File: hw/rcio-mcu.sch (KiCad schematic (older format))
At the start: 0 parts

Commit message: hw: start stm page
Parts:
- added C? (x5): 0.1, symbol Device:C
- added DD?: STM32F030CCTx, Package_QFP:LQFP-48_7x7mm_P0.5mm, symbol MCU_ST_STM32:STM32F030CCTx
- added XP?: stm_swdo, symbol dronecode_con:stm_swdo
- added XP?: FrSky-XSR, symbol dronecode_con:FrSky-XSR
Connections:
- net labels added: +3.3V, ADC_V5hat, ADC_Vbat, GND, HAT_CLK, RPI_SCL, RPI_SDA, RPI_SPI0_MISO, RPI_SPI0_MOSI, RPI_SPI0_SCLK, SERVO0, SERVO1, SERVO2, SERVO3, STM_BOOT0, SWCLK, SWDIO, SWO, ~NRST, ~RPI_SPI0_CE1, ~STM_INT, ~STM_RESET
- wire segments 0 -> 56
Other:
- note added: "NOTE: XSR module uses 5-pin conn.\nI decided to use 6-pin JST GH, to reduce nomenclature."

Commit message: hw: update libs
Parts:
- added C? (x2): 0.1, symbol Device:C
- added DA?: NCP361SN, symbol poweric:NCP361SN
- added R?: 10k, symbol Device:R
- XP?: symbol dronecode_con:stm_swdo -> dronecode-conn:stm_swdo
- XP?: symbol dronecode_con:FrSky-XSR -> dronecode-conn:FrSky-XSR
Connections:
- net labels added: +5VP, Rx_5V, Rx_CPPM, Rx_S.port, Rx_SBUS, ~Rx_EN
- wire segments 56 -> 72
- no-connect marks 0 -> 1
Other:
- moved on the sheet: XP?
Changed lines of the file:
@@
 $EndDescr
 $Comp
-L dronecode_con:stm_swdo XP?
+L dronecode-conn:stm_swdo XP?
 U 1 1 5AC130B8
-P 3450 8650
-F 0 "XP?" H 3678 8703 60  0000 L CNN
-F 1 "stm_swdo" H 3678 8597 60  0000 L CNN
-F 2 "" H 3450 8650 60  0001 C CNN
-F 3 "" H 3450 8650 60  0001 C CNN
-	1    3450 8650
+P 10500 8350
+F 0 "XP?" H 10728 8403 60  0000 L CNN
+F 1 "stm_swdo" H 10728 8297 60  0000 L CNN
+F 2 "" H 10500 8350 60  0001 C CNN
+F 3 "" H 10500 8350 60  0001 C CNN
+	1    10500 8350
 	1    0    0    -1
 $EndComp
@@
 L power:+3.3V #PWR?
 U 1 1 5AC3643C
-P 2900 8250
-F 0 "#PWR?" H 2900 8100 50  0001 C CNN
-F 1 "+3.3V" H 2915 8423 50  0000 C CNN
-F 2 "" H 2900 8250 50  0001 C CNN
-F 3 "" H 2900 8250 50  0001 C CNN
-	1    2900 8250
+P 9950 7950
+F 0 "#PWR?" H 9950 7800 50  0001 C CNN
+F 1 "+3.3V" H 9965 8123 50  0000 C CNN
+F 2 "" H 9950 7950 50  0001 C CNN
+F 3 "" H 9950 7950 50  0001 C CNN
+	1    9950 7950
 	1    0    0    -1
 $EndComp
@@
 L power:GND #PWR?
 U 1 1 5AC36455
-P 2900 9050
-F 0 "#PWR?" H 2900 8800 50  0001 C CNN
-F 1 "GND" H 2905 8877 50  0000 C CNN
-F 2 "" H 2900 9050 50  0001 C CNN
-F 3 "" H 2900 9050 50  0001 C CNN
-	1    2900 9050
-	1    0    0    -1
-$EndComp
-Wire Wire Line
-	3050 8400 2900 8400
-Wire Wire Line
-	2900 8400 2900 8250
-Wire Wire Line
-	3050 8600 2900 8600
-Wire Wire Line
-	2900 8600 2900 9050
-Wire Wire Line
-	3050 8500 2500 8500
-Wire Wire Line
-	3050 8700 2500 8700
-Wire Wire Line
-	3050 8800 2500 8800
-Wire Wire Line
-	3050 8900 2500 8900
-Text Label 2500 8500 0    60   ~ 0
+P 9950 8750
+F 0 "#PWR?" H 9950 8500 50  0001 C CNN
+F 1 "GND" H 9955 8577 50  0000 C CNN
+F 2 "" H 9950 8750 50  0001 C CNN
+F 3 "" H 9950 8750 50  0001 C CNN
+	1    9950 8750
+	1    0    0    -1
+$EndComp
+Wire Wire Line
+	10100 8100 9950 8100
+Wire Wire Line
+	9950 8100 9950 7950
+Wire Wire Line
+	10100 8300 9950 8300
+Wire Wire Line
+	9950 8300 9950 8750
+Wire Wire Line
+	10100 8200 9550 8200
+Wire Wire Line
+	10100 8400 9550 8400
+Wire Wire Line
+	10100 8500 9550 8500
+Wire Wire Line
+	10100 8600 9550 8600
+Text Label 9550 8200 0    60   ~ 0
 SWCLK
-Text Label 2500 8700 0    60   ~ 0
+Text Label 9550 8400 0    60   ~ 0
 SWDIO
-Text Label 2500 8800 0    60   ~ 0
+Text Label 9550 8500 0    60   ~ 0
 ~NRST
-Text Label 2500 8900 0    60   ~ 0
+Text Label 9550 8600 0    60   ~ 0
 SWO
 Text GLabel 3450 4850 0    60   Input ~ 0
@@
 Text GLabel 3500 6800 0    60   Output ~ 0
 SERVO3
-Text GLabel 3100 7300 0    60   UnSpc ~ 0
+Text GLabel 6350 6550 0    60   UnSpc ~ 0
 ADC_Vbat
-Text GLabel 3100 7400 0    60   UnSpc ~ 0
+Text GLabel 6350 6650 0    60   UnSpc ~ 0
 ADC_V5hat
 $Comp
-L dronecode_con:FrSky-XSR XP?
+L dronecode-conn:FrSky-XSR XP?
 U 1 1 5AC46946
-P 7500 8650
-F 0 "XP?" H 7728 8703 60  0000 L CNN
-F 1 "FrSky-XSR" H 7728 8597 60  0000 L CNN
-F 2 "" H 7500 8650 60  0001 C CNN
-F 3 "" H 7500 8650 60  0001 C CNN
-	1    7500 8650
-	1    0    0    -1
-$EndComp
-Text Notes 7250 9350 0    60   ~ 0
+P 5350 7950
+F 0 "XP?" H 5578 8003 60  0000 L CNN
+F 1 "FrSky-XSR" H 5578 7897 60  0000 L CNN
+F 2 "" H 5350 7950 60  0001 C CNN
+F 3 "" H 5350 7950 60  0001 C CNN
+	1    5350 7950
+	1    0    0    -1
+$EndComp
+Text Notes 4250 8800 0    60   ~ 0
 NOTE: XSR module uses 5-pin conn.\nI decided to use 6-pin JST GH, to reduce nomenclature.
 $Comp
 L power:GND #PWR?
 U 1 1 5AC47AE2
-P 7000 9000
-F 0 "#PWR?" H 7000 8750 50  0001 C CNN
-F 1 "GND" H 7005 8827 50  0000 C CNN
-F 2 "" H 7000 9000 50  0001 C CNN
-F 3 "" H 7000 9000 50  0001 C CNN
-	1    7000 9000
-	1    0    0    -1
-$EndComp
-Wire Wire Line
-	7100 8800 7000 8800
-Wire Wire Line
-	7000 8800 7000 8900
-Wire Wire Line
-	7100 8900 7000 8900
-Connection ~ 7000 8900
-Wire Wire Line
-	7000 8900 7000 9000
-Wire Wire Line
-	7100 8400 6500 8400
-Wire Wire Line
-	7100 8500 6500 8500
-Wire Wire Line
-	7100 8600 6500 8600
+P 4850 8300
+F 0 "#PWR?" H 4850 8050 50  0001 C CNN
+F 1 "GND" H 4855 8127 50  0000 C CNN
+F 2 "" H 4850 8300 50  0001 C CNN
+F 3 "" H 4850 8300 50  0001 C CNN
+	1    4850 8300
+	1    0    0    -1
+$EndComp
+Wire Wire Line
+	4950 8100 4850 8100
+Wire Wire Line
+	4850 8100 4850 8200
+Wire Wire Line
+	4950 8200 4850 8200
+Connection ~ 4850 8200
+Wire Wire Line
+	4850 8200 4850 8300
+Wire Wire Line
+	4950 7700 4350 7700
+Wire Wire Line
+	4950 7800 4350 7800
+Wire Wire Line
+	4950 7900 4350 7900
+$Comp
+L poweric:NCP361SN DA?
+U 1 1 5AC5BECB
+P 3300 8300
+F 0 "DA?" H 3100 8750 60  0000 C CNN
+F 1 "NCP361SN" H 3350 7900 60  0000 C CNN
+F 2 "" H 3300 8300 60  0000 C CNN
+F 3 "http://www.onsemi.com/pub_link/Collateral/NCP361-D.PDF" H 4350 7400 60  0000 C CNN
+	1    3300 8300
+	1    0    0    -1
+$EndComp
+$Comp
+L power:GND #PWR?
+U 1 1 5AC5C395
+P 3900 8750
+F 0 "#PWR?" H 3900 8500 50  0001 C CNN
+F 1 "GND" H 3905 8577 50  0000 C CNN
+F 2 "" H 3900 8750 50  0001 C CNN
+F 3 "" H 3900 8750 50  0001 C CNN
+	1    3900 8750
+	1    0    0    -1
+$EndComp
+$Comp
+L power:GND #PWR?
+U 1 1 5AC5C3B2
+P 2550 9100
+F 0 "#PWR?" H 2550 8850 50  0001 C CNN
+F 1 "GND" H 2555 8927 50  0000 C CNN
+F 2 "" H 2550 9100 50  0001 C CNN
+F 3 "" H 2550 9100 50  0001 C CNN
+	1    2550 9100
+	1    0    0    -1
+$EndComp
+$Comp
+L Device:R R?
+U 1 1 5AC5C5BF
+P 2550 8750
+F 0 "R?" H 2620 8796 50  0000 L CNN
+F 1 "10k" H 2620 8705 50  0000 L CNN
+F 2 "" V 2480 8750 50  0001 C CNN
+F 3 "~" H 2550 8750 50  0001 C CNN
+	1    2550 8750
+	1    0    0    -1
+$EndComp
+Wire Wire Line
+	2800 8450 2550 8450
+Wire Wire Line
+	2550 8600 2550 8450
+Connection ~ 2550 8450
+Wire Wire Line
+	2550 8450 2350 8450
+Wire Wire Line
+	2550 8900 2550 9000
+Wire Wire Line
+	3800 8550 3900 8550
+Wire Wire Line
+	3900 8550 3900 8750
+Wire Wire Line
+	4950 8000 3900 8000
+Text Label 4000 8000 0    60   ~ 0
+Rx_5V
+Text Label 4350 7700 0    60   ~ 0
+Rx_SBUS
+Text Label 4350 7800 0    60   ~ 0
+Rx_CPPM
+Text Label 4350 7900 0    60   ~ 0
+Rx_S.port
+$Comp
+L power:+5VP #PWR?
+U 1 1 5AC6272A
+P 2250 7900
+F 0 "#PWR?" H 2250 7750 50  0001 C CNN
+F 1 "+5VP" H 2265 8073 50  0000 C CNN
+F 2 "" H 2250 7900 50  0001 C CNN
+F 3 "" H 2250 7900 50  0001 C CNN
+	1    2250 7900
+	1    0    0    -1
+$EndComp
+$Comp
+L Device:C C?
+U 1 1 5AC63063
+P 2250 8750
+F 0 "C?" H 2365 8796 50  0000 L CNN
+F 1 "0.1" H 2365 8705 50  0000 L CNN
+F 2 "" H 2288 8600 50  0001 C CNN
+F 3 "~" H 2250 8750 50  0001 C CNN
+	1    2250 8750
+	1    0    0    -1
+$EndComp
+$Comp
+L Device:C C?
+U 1 1 5AC631FE
+P 3900 8250
+F 0 "C?" H 4015 8296 50  0000 L CNN
+F 1 "0.1" H 4015 8205 50  0000 L CNN
+F 2 "" H 3938 8100 50  0001 C CNN
+F 3 "~" H 3900 8250 50  0001 C CNN
+	1    3900 8250
+	1    0    0    -1
+$EndComp
+Wire Wire Line
+	3900 8000 3900 8100
+Connection ~ 3900 8000
+Wire Wire Line
+	3900 8000 3800 8000
+Wire Wire Line
+	3900 8400 3900 8550
+Connection ~ 3900 8550
+Wire Wire Line
+	2550 9000 2250 9000
+Wire Wire Line
+	2250 9000 2250 8900
+Connection ~ 2550 9000
+Wire Wire Line
+	2550 9000 2550 9100
+Text Label 2350 8450 0    60   ~ 0
+~Rx_EN
+Wire Wire Line
+	2250 7900 2250 8000
+Wire Wire Line
+	2800 8000 2250 8000
+Connection ~ 2250 8000
+Wire Wire Line
+	2250 8000 2250 8600
+NoConn ~ 2800 8550
 $EndSCHEMATC

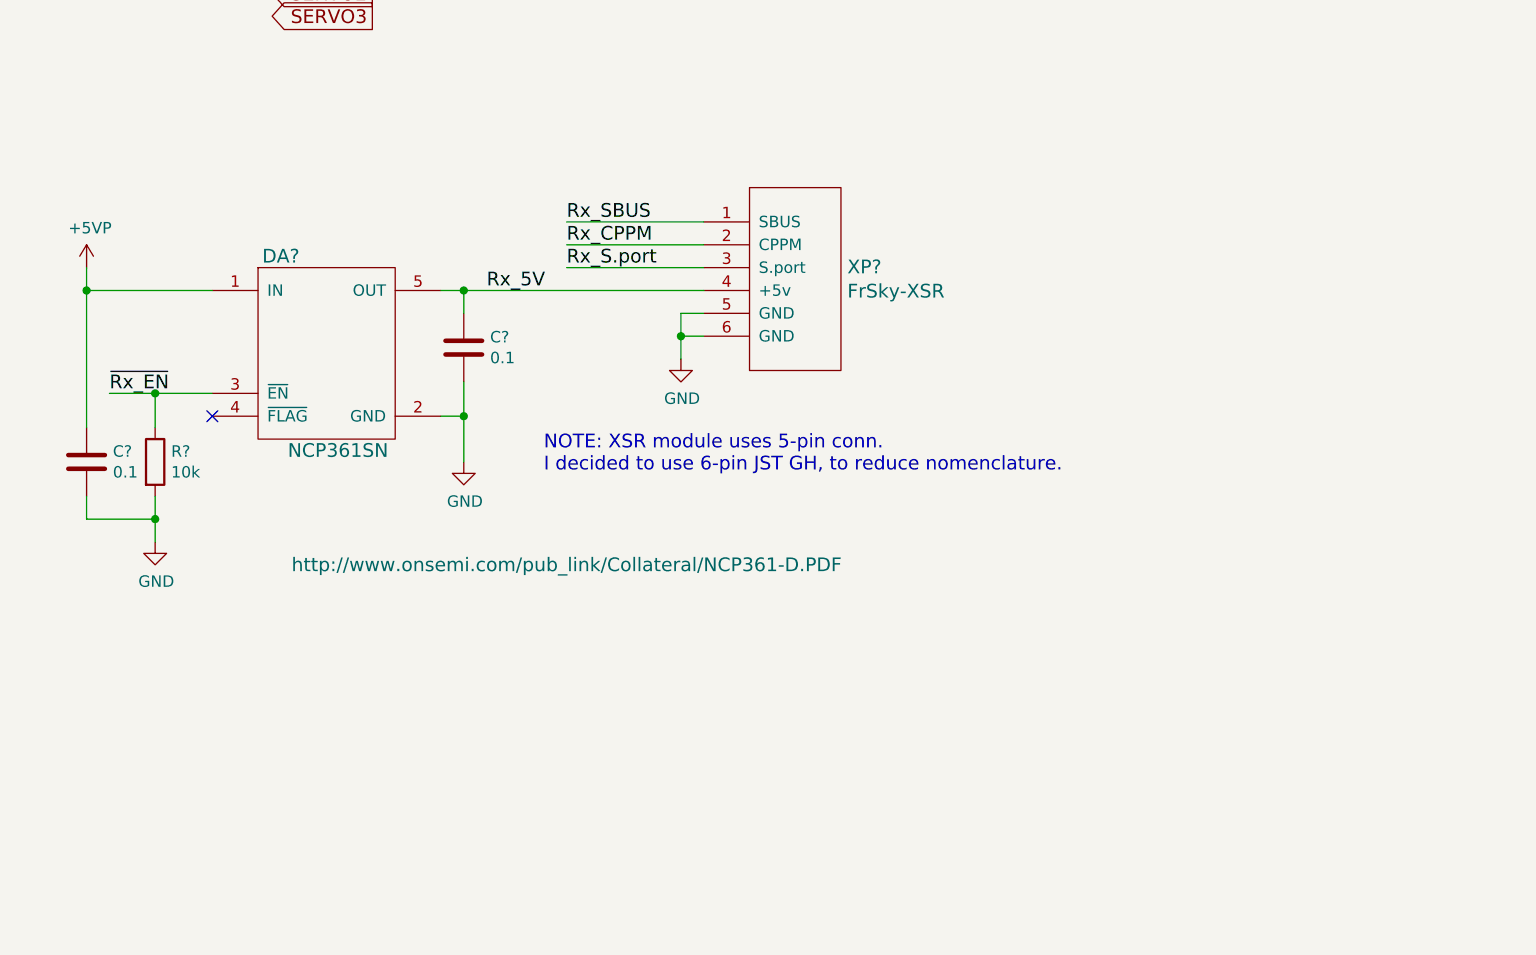
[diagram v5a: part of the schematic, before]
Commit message: hw: add CPPM source switch
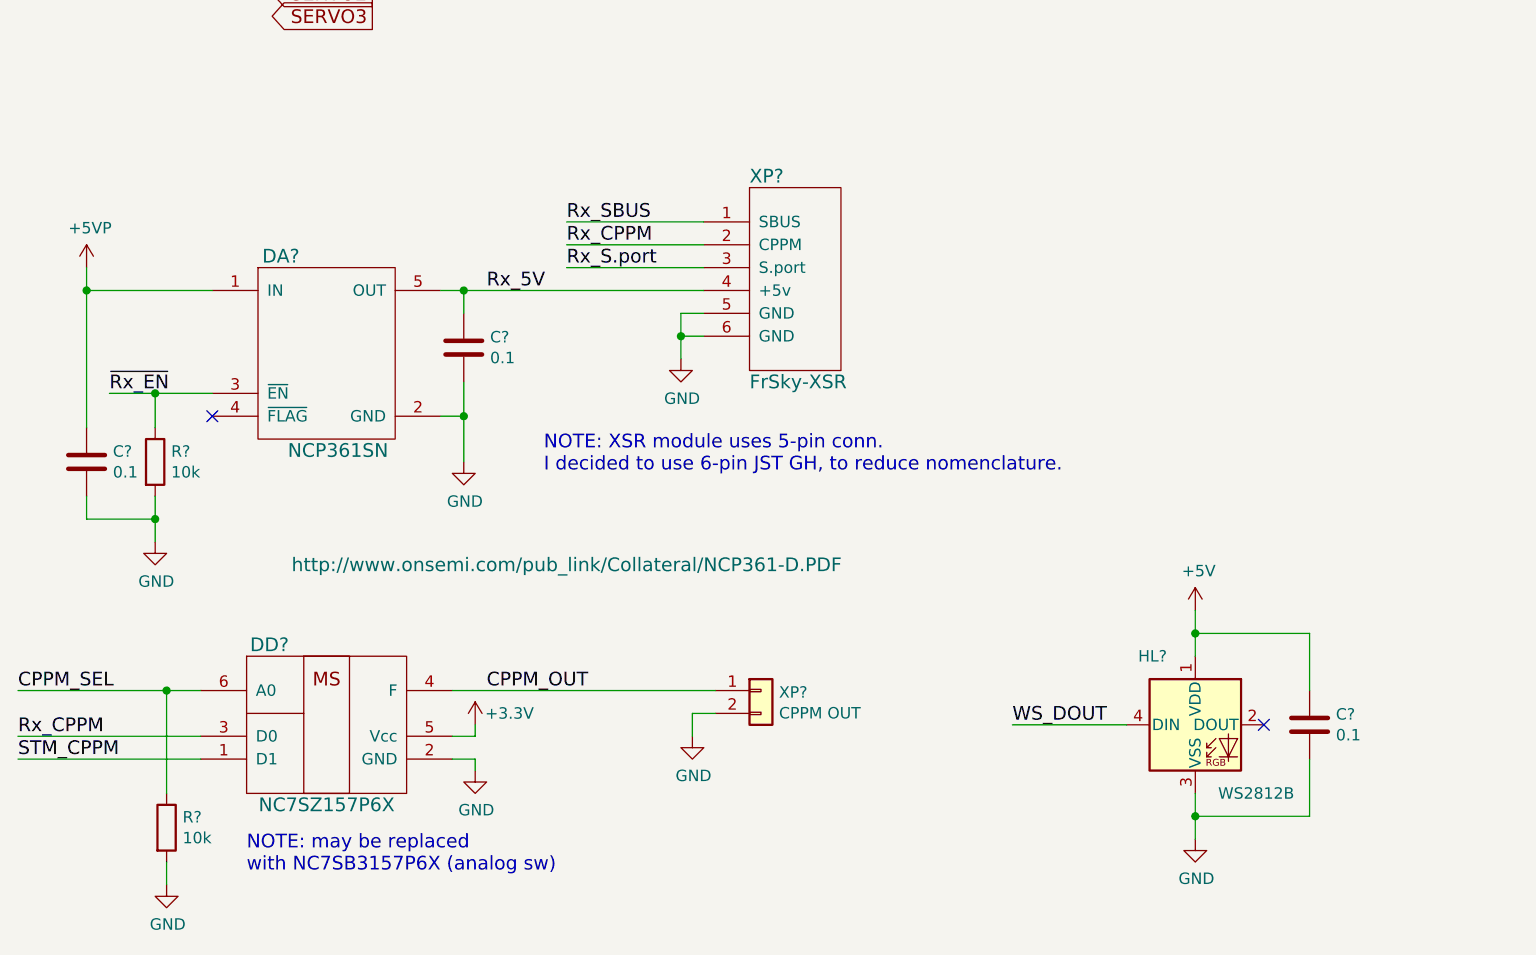
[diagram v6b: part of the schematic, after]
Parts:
- added C?: 0.1, symbol Device:C
- added DD?: NC7SZ157P6X, symbol hat-ic:NC7SZ157P6X
- added HL?: WS2812B, LED_SMD:LED_WS2812B_PLCC4_5.0x5.0mm_P3.2mm, symbol LED:WS2812B
- added R?: 10k, symbol Device:R
- added XP?: CPPM OUT, symbol Connector_Generic:Conn_01x02
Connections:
- net +3V3: now also DD?.5 (Vcc)
- net GND: now also C?.2, DD?.2 (GND), HL?.3 (VSS), R?.2, XP?.2 (Pin_2)
- net Rx_CPPM: now also DD?.3 (D0)
- new net +5V: C?.1, HL?.1 (VDD)
- new net CPPM_OUT: DD?.4 (F), XP?.1 (Pin_1)
- new net CPPM_SEL: DD?.6 (A0), R?.1
- new net STM_CPPM: DD?.1 (D1)
- new net WS_DOUT: HL?.4 (DIN)
- no-connect marks 1 -> 2
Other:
- note added: "NOTE: may be replaced\nwith NC7SB3157P6X (analog sw)"
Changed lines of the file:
@@
 U 1 1 5AC46946
 P 5350 7950
-F 0 "XP?" H 5578 8003 60  0000 L CNN
-F 1 "FrSky-XSR" H 5578 7897 60  0000 L CNN
+F 0 "XP?" H 5150 8400 60  0000 L CNN
+F 1 "FrSky-XSR" H 5150 7500 60  0000 L CNN
 F 2 "" H 5350 7950 60  0001 C CNN
 F 3 "" H 5350 7950 60  0001 C CNN
@@
 	2250 8000 2250 8600
 NoConn ~ 2800 8550
+$Comp
+L hat-ic:NC7SZ157P6X DD?
+U 1 1 5AC7BF22
+P 3300 9950
+F 0 "DD?" H 3050 10350 60  0000 C CNN
+F 1 "NC7SZ157P6X" H 3300 9650 60  0000 C CNN
+F 2 "" H 3300 9950 60  0001 C CNN
+F 3 "https://www.terraelectronica.ru/pdf/show?pdf_file=%252Fds%252Fpdf%252FN%252Fnc7sz157p6x.pdf" H 3300 9950 60  0001 C CNN
+	1    3300 9950
+	1    0    0    -1
+$EndComp
+Wire Wire Line
+	2750 9950 1950 9950
+Text Label 1950 9950 0    60   ~ 0
+Rx_CPPM
+Text Notes 2950 10550 0    60   ~ 0
+NOTE: may be replaced\nwith NC7SB3157P6X (analog sw)
+Wire Wire Line
+	3850 9750 5000 9750
+Text Label 4000 9750 0    60   ~ 0
+CPPM_OUT
+$Comp
+L power:GND #PWR?
+U 1 1 5AC8062A
+P 3950 10100
+F 0 "#PWR?" H 3950 9850 50  0001 C CNN
+F 1 "GND" H 3955 9927 50  0000 C CNN
+F 2 "" H 3950 10100 50  0001 C CNN
+F 3 "" H 3950 10100 50  0001 C CNN
+	1    3950 10100
+	1    0    0    -1
+$EndComp
+$Comp
+L power:+3.3V #PWR?
+U 1 1 5AC80AAD
+P 3950 9900
+F 0 "#PWR?" H 3950 9750 50  0001 C CNN
+F 1 "+3.3V" H 4100 9950 50  0000 C CNN
+F 2 "" H 3950 9900 50  0001 C CNN
+F 3 "" H 3950 9900 50  0001 C CNN
+	1    3950 9900
+	1    0    0    -1
+$EndComp
+Wire Wire Line
+	3850 9950 3950 9950
+Wire Wire Line
+	3950 9950 3950 9900
+Wire Wire Line
+	3950 10100 3950 10050
+Wire Wire Line
+	3950 10050 3850 10050
+$Comp
+L Device:R R?
+U 1 1 5AC852D0
+P 2600 10350
+F 0 "R?" H 2670 10396 50  0000 L CNN
+F 1 "10k" H 2670 10305 50  0000 L CNN
+F 2 "" V 2530 10350 50  0001 C CNN
+F 3 "~" H 2600 10350 50  0001 C CNN
+	1    2600 10350
+	1    0    0    -1
+$EndComp
+$Comp
+L power:GND #PWR?
+U 1 1 5AC85376
+P 2600 10600
+F 0 "#PWR?" H 2600 10350 50  0001 C CNN
+F 1 "GND" H 2605 10427 50  0000 C CNN
+F 2 "" H 2600 10600 50  0001 C CNN
+F 3 "" H 2600 10600 50  0001 C CNN
+	1    2600 10600
+	1    0    0    -1
+$EndComp
+Wire Wire Line
+	2750 9750 2600 9750
+Text Label 1950 9750 0    60   ~ 0
+CPPM_SEL
+Wire Wire Line
+	2750 10050 1950 10050
+Wire Wire Line
+	2600 10200 2600 9750
+Connection ~ 2600 9750
+Wire Wire Line
+	2600 9750 1950 9750
+Wire Wire Line
+	2600 10500 2600 10600
+Text Label 1950 10050 0    60   ~ 0
+STM_CPPM
+$Comp
+L Connector_Generic:Conn_01x02 XP?
+U 1 1 5AC8F981
+P 5200 9750
+F 0 "XP?" H 5279 9742 50  0000 L CNN
+F 1 "CPPM OUT" H 5279 9651 50  0000 L CNN
+F 2 "" H 5200 9750 50  0001 C CNN
+F 3 "~" H 5200 9750 50  0001 C CNN
+	1    5200 9750
+	1    0    0    -1
+$EndComp
+$Comp
+L power:GND #PWR?
+U 1 1 5AC91D74
+P 4900 9950
+F 0 "#PWR?" H 4900 9700 50  0001 C CNN
+F 1 "GND" H 4905 9777 50  0000 C CNN
+F 2 "" H 4900 9950 50  0001 C CNN
+F 3 "" H 4900 9950 50  0001 C CNN
+	1    4900 9950
+	1    0    0    -1
+$EndComp
+Wire Wire Line
+	5000 9850 4900 9850
+Wire Wire Line
+	4900 9850 4900 9950
+$Comp
+L LED:WS2812B HL?
+U 1 1 5AC97EF6
+P 7100 9900
+F 0 "HL?" H 6850 10200 50  0000 L CNN
+F 1 "WS2812B" H 7200 9600 50  0000 L CNN
+F 2 "LED_SMD:LED_WS2812B_PLCC4_5.0x5.0mm_P3.2mm" H 7150 9600 50  0001 L TNN
+F 3 "https://cdn-shop.adafruit.com/datasheets/WS2812B.pdf" H 7200 9525 50  0001 L TNN
+	1    7100 9900
+	1    0    0    -1
+$EndComp
+$Comp
+L power:GND #PWR?
+U 1 1 5AC98B02
+P 7100 10400
+F 0 "#PWR?" H 7100 10150 50  0001 C CNN
+F 1 "GND" H 7105 10227 50  0000 C CNN
+F 2 "" H 7100 10400 50  0001 C CNN
+F 3 "" H 7100 10400 50  0001 C CNN
+	1    7100 10400
+	1    0    0    -1
+$EndComp
+$Comp
+L power:+5V #PWR?
+U 1 1 5AC98E44
+P 7100 9400
+F 0 "#PWR?" H 7100 9250 50  0001 C CNN
+F 1 "+5V" H 7115 9573 50  0000 C CNN
+F 2 "" H 7100 9400 50  0001 C CNN
+F 3 "" H 7100 9400 50  0001 C CNN
+	1    7100 9400
+	1    0    0    -1
+$EndComp
+Wire Wire Line
+	7100 9600 7100 9500
+Wire Wire Line
+	7100 10200 7100 10300
+NoConn ~ 7400 9900
+Wire Wire Line
+	6800 9900 6300 9900
+Text Label 6300 9900 0    60   ~ 0
+WS_DOUT
+$Comp
+L Device:C C?
+U 1 1 5ACA99A8
+P 7600 9900
+F 0 "C?" H 7715 9946 50  0000 L CNN
+F 1 "0.1" H 7715 9855 50  0000 L CNN
+F 2 "" H 7638 9750 50  0001 C CNN
+F 3 "~" H 7600 9900 50  0001 C CNN
+	1    7600 9900
+	1    0    0    -1
+$EndComp
+Wire Wire Line
+	7100 9500 7600 9500
+Wire Wire Line
+	7600 9500 7600 9750
+Connection ~ 7100 9500
+Wire Wire Line
+	7100 9500 7100 9400
+Wire Wire Line
+	7100 10300 7600 10300
+Wire Wire Line
+	7600 10300 7600 10050
+Connection ~ 7100 10300
+Wire Wire Line
+	7100 10300 7100 10400
 $EndSCHEMATC

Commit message: hw: complete mcu sheet
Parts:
- added R? (x4): 10k, symbol Device:R
- added R?: 47k, symbol Device:R
- added R?: 4.7k, symbol Device:R
- added VT?: DMG2305UX, TO_SOT_Packages_SMD:SOT-23_Handsoldering, symbol hat-ic:DMG2305UX
- added XP?: DBG UART, symbol Connector_Generic:Conn_01x03
- added XP?: FAN, symbol Connector_Generic:Conn_01x02
- XP?: value stm_swdo -> SWD
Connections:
- net +5V: now also R?.1, VT?.2 (S)
- net ADC_V5hat: now also R?.1
- net ADC_Vbat: now also R?.1
- net CPPM_SEL: now also DD?.41 (PB5/I2C1_SMBA/SPI1_MOSI/TIM16_BKIN/TIM3_CH2/USART5_CK/USART5_DE/USART5_RTS)
- net GND: now also R?.2, R?.2, R?.2, XP?.2 (Pin_2), XP?.3 (Pin_3)
- net RPI_SCL: now also DD?.42 (PB6/I2C1_SCL/TIM16_CH1N/USART1_TX)
- net RPI_SDA: now also DD?.43 (PB7/I2C1_SDA/TIM17_CH1N/USART1_RX/USART4_CTS)
- net RPI_SPI0_MISO: now also DD?.16 (ADC_IN6/SPI1_MISO/TIM16_CH1/TIM1_BKIN/TIM3_CH1/USART3_CTS/PA6)
- net RPI_SPI0_MOSI: now also DD?.17 (ADC_IN7/SPI1_MOSI/TIM14_CH1/TIM17_CH1/TIM1_CH1N/TIM3_CH2/PA7)
- net RPI_SPI0_SCLK: now also DD?.15 (ADC_IN5/SPI1_SCK/USART6_RX/PA5)
- net Rx_S.port: now also DD?.21 (PB10/I2C2_SCL/SPI2_SCK/USART3_TX)
- net Rx_SBUS: now also DD?.12 (ADC_IN2/TIM15_CH1/USART2_TX/PA2)
- net SERVO0: now also DD?.29 (RCC_MCO/TIM1_CH1/USART1_CK/PA8)
- net SERVO1: now also DD?.28 (PB15/RTC_REFIN/SPI2_MOSI/TIM15_CH1N/TIM15_CH2/TIM1_CH3N)
- net SERVO2: now also DD?.27 (PB14/I2C2_SDA/SPI2_MISO/TIM15_CH1/TIM1_CH2N/USART3_DE/USART3_RTS)
- net SERVO3: now also DD?.32 (I2C2_SCL/TIM1_CH4/USART1_CTS/PA11)
- net STM_BOOT0: now also R?.1
- net STM_CPPM: now also DD?.40 (PB4/SPI1_MISO/TIM17_BKIN/TIM3_CH1/USART5_RX)
- net SWCLK: now also DD?.37 (SYS_SWCLK/USART2_TX/PA14)
- net SWDIO: now also DD?.34 (IR_OUT/SYS_SWDIO/PA13)
- net WS_DOUT: now also DD?.39 (PB3/SPI1_SCK/USART5_TX)
- net ~RPI_SPI0_CE1: now also DD?.14 (ADC_IN4/SPI1_NSS/TIM14_CH1/USART2_CK/USART6_TX/PA4)
- net ~Rx_EN: now also DD?.38 (SPI1_NSS/USART2_RX/USART4_DE/USART4_RTS/PA15)
- net ~STM_INT: now also DD?.18 (PB0/ADC_IN8/TIM1_CH2N/TIM3_CH3/USART3_CK)
- net ADC_IN0_Vbat: now reaches DD?.10 (ADC_IN0/RTC_TAMP2/SYS_WKUP1/USART2_CTS/USART4_TX/PA0)
- net ADC_IN0_Vbat: now also R?.1, R?.2
- net ADC_IN1_5V: now reaches DD?.11 (ADC_IN1/TIM15_CH1N/USART2_DE/USART2_RTS/USART4_RX/PA1)
- net ADC_IN1_5V: now also R?.1, R?.2
- net STM_U1_TX: now reaches DD?.30 (I2C1_SCL/RCC_MCO/TIM15_BKIN/TIM1_CH2/USART1_TX/PA9)
- net STM_U1_TX: now also XP?.1 (Pin_1)
- net STM_U1_RX: now reaches DD?.31 (I2C1_SDA/TIM17_BKIN/TIM1_CH3/USART1_RX/PA10)
- net STM_U1_RX: now also XP?.2 (Pin_2)
- net ~FAN_PWM: now reaches DD?.45 (PB8/I2C1_SCL/TIM16_CH1)
- net ~FAN_PWM: now also R?.2, VT?.1 (G)
- net SWO: no longer names the net of XP?.6 (SWO)
- new net FAN+: VT?.3 (D), XP?.1 (Pin_1)
- no-connect marks 2 -> 15
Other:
- note added: "NOTE: For rev.1 will use same transistor as for ZVD.\nBut that limit to 5V only FANs."
- moved on the sheet: C?, DA?, DD?, HL?, R?, XP?

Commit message: hw: add note
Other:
- note added: "NOTE: WS_DOUT can be implemented\non TIM17 CH1 (PB9), or USART5 (PB3).\n\nDecided to leave only USART5 because\ni implemented usart based driver prev."
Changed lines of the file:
@@
 NoConn ~ 6650 2750
 NoConn ~ 6650 2550
+Text Notes 6850 5750 0    60   ~ 0
+NOTE: WS_DOUT can be implemented\non TIM17 CH1 (PB9), or USART5 (PB3).\n\nDecided to leave only USART5 because\ni implemented usart based driver prev.
 $EndSCHEMATC
